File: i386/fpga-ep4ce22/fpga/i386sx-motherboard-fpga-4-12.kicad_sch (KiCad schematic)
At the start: 1 part, among them U14 SN74LVC8T245PWR

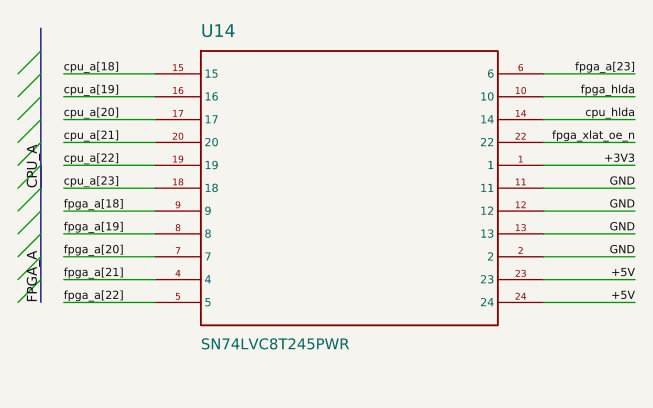
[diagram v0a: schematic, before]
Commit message: Publish the motherboards' KiCad files
From socket3@c0f6464 socket7@9205469 socket370@524f5b1 i386@bea926c
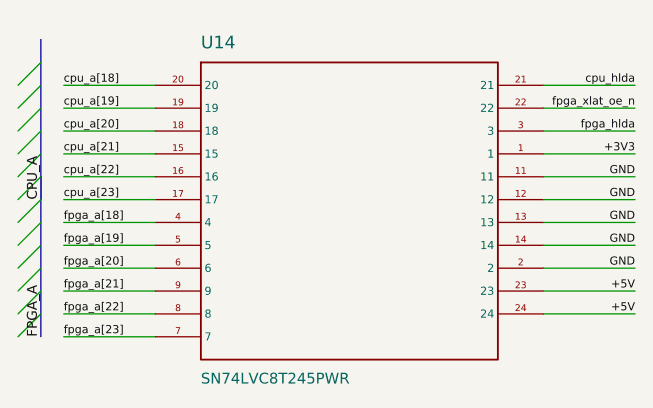
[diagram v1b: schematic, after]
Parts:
- removed U14: SN74LVC8T245PWR, symbol gen:S11_11
- added U14: SN74LVC8T245PWR, symbol gen:S12_11
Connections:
- net +3V3: now also U14.1
- net +5V: now also U14.23, U14.24
- net GND: now also U14.11, U14.12, U14.13, U14.14, U14.2
- net cpu_a[18]: now also U14.20
- net cpu_a[19]: now also U14.19
- net cpu_a[20]: now also U14.18
- net cpu_a[21]: now also U14.15
- net cpu_a[22]: now also U14.16
- net cpu_a[23]: now also U14.17
- net cpu_hlda: now also U14.21
- net fpga_a[18]: now also U14.4
- net fpga_a[19]: now also U14.5
- net fpga_a[20]: now also U14.6
- net fpga_a[21]: now also U14.9
- net fpga_a[22]: now also U14.8
- net fpga_a[23]: now also U14.7
- net fpga_hlda: now also U14.3
- net fpga_xlat_oe_n: now also U14.22
